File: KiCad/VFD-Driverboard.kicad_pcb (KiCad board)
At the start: 2 copper layers, 100 x 25 mm, 2 parts, among them J2 Breadboard

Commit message: new PCB
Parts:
- removed J2: Breadboard, Connector_PinHeader_2.54mm:PinHeader_1x10_P2.54mm_Vertical
- added C1: 1u, Capacitor_SMD:C_2220_5750Metric_Pad1.97x5.40mm_HandSolder, B.Cu at (35.1, 27.5)
- added C2: 10n, Capacitor_SMD:C_1206_3216Metric_Pad1.33x1.80mm_HandSolder, B.Cu at (53.3, 32.4)
- added C3: 1u, Capacitor_SMD:C_2220_5750Metric_Pad1.97x5.40mm_HandSolder, B.Cu at (107.2, 30.3)
- added C4: 1u, Capacitor_SMD:C_2220_5750Metric_Pad1.97x5.40mm_HandSolder, B.Cu at (21.1, 30.2)
- added C5: 1u, Capacitor_SMD:C_2220_5750Metric_Pad1.97x5.40mm_HandSolder, B.Cu at (54.7, 24.0)
- added C6: 100uF, Capacitor_Tantalum_SMD:CP_EIA-7343-31_Kemet-D_Pad2.25x2.55mm_HandSolder, B.Cu at (64.2, 34.5)
- added C7: 270pF, Capacitor_SMD:C_1206_3216Metric_Pad1.33x1.80mm_HandSolder, B.Cu at (76.5, 38.0)
- added C8: 100uF, Capacitor_Tantalum_SMD:CP_EIA-7343-31_Kemet-D_Pad2.25x2.55mm_HandSolder, B.Cu at (99.6, 34.6)
- added C9: 82p, Capacitor_SMD:C_1206_3216Metric_Pad1.33x1.80mm_HandSolder, F.Cu at (93.3, 24.9)
- added D1: 2V7, Diode_SMD:D_2010_5025Metric_Pad1.52x2.65mm_HandSolder, B.Cu at (63.2, 22.6)
- added D2: 1N5819, Diode_SMD:D_SOD-123, B.Cu at (93.4, 31.2)
- added D3: D, Diode_SMD:D_2010_5025Metric_Pad1.52x2.65mm_HandSolder, B.Cu at (63.2, 27.1)
- added G***: LOGO, MyLib:Salamander_Silk, F.Cu at (105.0, 32.5)
- added G***: LOGO, MyLib:Salamander_B_Copper, F.Cu at (32.0, 33.6)
- added H1: MountingHole, MountingHole:MountingHole_3.2mm_M3_ISO14580_Pad_TopBottom, F.Cu at (17.2, 17.0)
- added H2: MountingHole, MountingHole:MountingHole_3.2mm_M3_ISO14580_Pad_TopBottom, F.Cu at (109.7, 17.0)
- added H3: MountingHole, MountingHole:MountingHole_3.2mm_M3_ISO14580_Pad_TopBottom, F.Cu at (17.2, 45.0)
- added H4: MountingHole, MountingHole:MountingHole_3.2mm_M3_ISO14580_Pad_TopBottom, F.Cu at (109.5, 45.0)
- added J1: MCU, Connector_PinSocket_2.54mm:PinSocket_1x08_P2.54mm_Vertical, F.Cu at (100.2, 16.4)
- added L1: 100uH, MyLib:IND_TAIYO_NRS8040_TAY, B.Cu at (77.8, 24.5)
- added R1: 10k, Resistor_SMD:R_1206_3216Metric_Pad1.30x1.75mm_HandSolder, B.Cu at (43.9, 32.3)
- added R10: 47k, Resistor_SMD:R_1206_3216Metric_Pad1.30x1.75mm_HandSolder, F.Cu at (99.6, 24.9)
- added R11: 1k8, Resistor_SMD:R_1206_3216Metric_Pad1.30x1.75mm_HandSolder, F.Cu at (99.6, 28.5)
- added R12: 8k2, Resistor_SMD:R_1206_3216Metric_Pad1.30x1.75mm_HandSolder, F.Cu at (93.3, 28.5)
- added R2: 10k, Resistor_SMD:R_1206_3216Metric_Pad1.30x1.75mm_HandSolder, B.Cu at (53.3, 28.8)
- added R3: 2k2, Resistor_SMD:R_1206_3216Metric_Pad1.30x1.75mm_HandSolder, B.Cu at (43.9, 35.9)
- added R4: 10k, Resistor_SMD:R_1206_3216Metric_Pad1.30x1.75mm_HandSolder, B.Cu at (43.9, 22.2)
- added R5: 1k, Resistor_SMD:R_1206_3216Metric_Pad1.30x1.75mm_HandSolder, F.Cu at (107.2, 24.9)
- added R6: 1k, Resistor_SMD:R_1206_3216Metric_Pad1.30x1.75mm_HandSolder, F.Cu at (21.1, 24.8)
- added R7: 100k, Resistor_SMD:R_1206_3216Metric_Pad1.30x1.75mm_HandSolder, B.Cu at (53.3, 35.9)
- added R8: 1, Resistor_SMD:R_1206_3216Metric_Pad1.30x1.75mm_HandSolder, B.Cu at (70.3, 38.0)
- added R9: 180, Resistor_SMD:R_1206_3216Metric_Pad1.30x1.75mm_HandSolder, B.Cu at (70.2, 34.5)
- added TP1: VEE, TestPoint:TestPoint_Pad_D2.5mm, B.Cu at (63.4, 16.9)
- added TP2: F-, TestPoint:TestPoint_Pad_D2.5mm, B.Cu at (104.2, 17.0)
- added TP3: F+, TestPoint:TestPoint_Pad_D2.5mm, B.Cu at (23.3, 16.9)
- added U1: MC34063, MyLib:SOIC127P599X175-8N, B.Cu at (77.7, 32.9)
- added U2: LM4871, MyLib:SOIC127P599X175-8N, B.Cu at (44.0, 27.2)
- V1: value ~ -> HCS-12SS59T
- moved V1 5.44 mm to (13.4, 19.4)
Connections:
- V1 pad 7: GNDD -> Gnd
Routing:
- net Net-(D1-K): track 0.00 -> 99.3 mm, vias 0 -> 4
- net Net-(U2-V01): track 0.00 -> 90.2 mm, vias 0 -> 2
- net VCC: track 35.2 -> 88.6 mm, vias 0 -> 1
- net Net-(D3-K): track 0.00 -> 48.1 mm
- net Gnd: track 0.00 -> 46.5 mm
- net Net-(U1-GND): track 0.00 -> 40.0 mm, vias 0 -> 1
- net GNDD: track 36.1 -> 0.00 mm
- net Net-(J1-Pin_8): track 38.8 -> 6.24 mm
- net Net-(J1-Pin_7): track 38.3 -> 6.01 mm
- net Net-(U1-Vfb): track 0.00 -> 32.3 mm, vias 0 -> 1
- net Net-(J1-Pin_6): track 37.7 -> 5.79 mm
- net Net-(J1-Pin_5): track 37.2 -> 5.57 mm
- net VF2: track 40.8 -> 16.5 mm, vias 0 -> 1
- net VF1: track 40.4 -> 16.2 mm, vias 0 -> 1
- net Net-(J1-Pin_4): track 36.7 -> 13.1 mm
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- added copper zone on B.Cu, net Gnd
- added copper zone on F.Cu, net Gnd
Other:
- board size 100 x 25 mm -> 100 x 35 mm
- board text added: "VFD driver board for Samsung HCS-12SS59T (c) 2024 rlnd HW-Rev. 1.1.0"

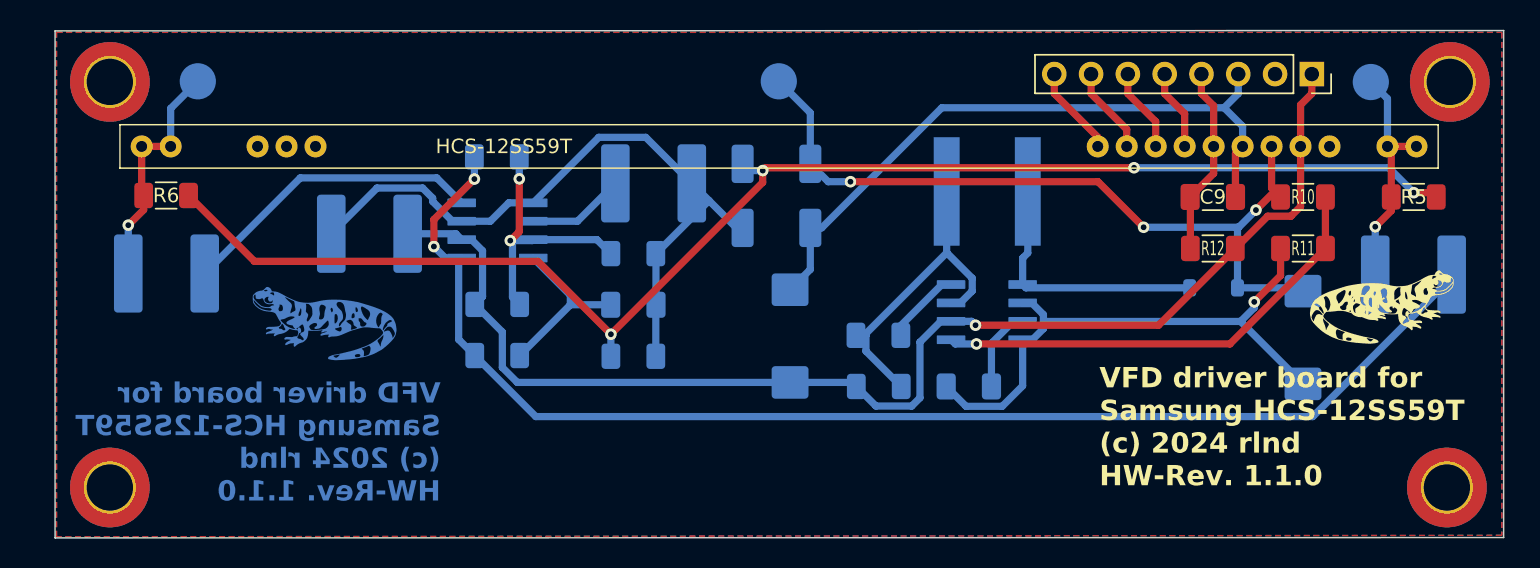
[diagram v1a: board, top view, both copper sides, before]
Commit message: added MPLAB project
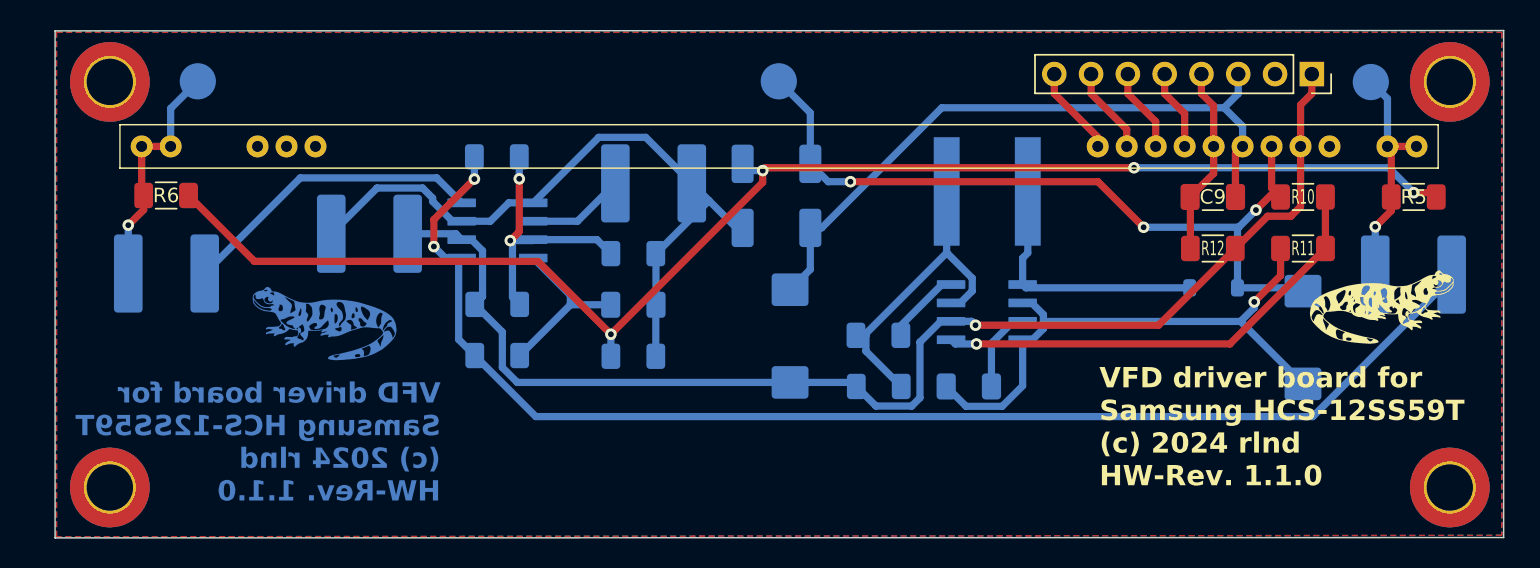
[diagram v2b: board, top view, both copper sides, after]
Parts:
- TP1: value VEE -> Vee
- U1: value MC34063 -> MC34063AD
- U2: value LM4871 -> LM4871MX_NOPB
- V1: value HCS-12SS59T -> ~
- moved H4 0.20 mm to (109.7, 45.0)
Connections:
- C1 pad 2: Net-(D3-K) -> Net-(U2-GND)
- C2 pad 2: Net-(D3-K) -> Net-(U2-GND)
- C5 pad 2: Net-(D3-K) -> Net-(U2-GND)
- J1 pad 3: Gnd -> Net-(J1-Pin_3)
- R7 pad 2: Net-(D3-K) -> Net-(U2-GND)
- U2 pad 1: Net-(D3-K) -> unconnected-(U2-SHUTDOWN-Pad1)
- U2 pad 7: Net-(D3-K) -> Net-(U2-GND)
- V1 pad 7: Gnd -> Net-(J1-Pin_3)
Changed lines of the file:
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@@
 		(allow_soldermask_bridges_in_footprints no)
 		(pcbplotparams
-			(layerselection 0x0001000_fffffffe)
+			(layerselection 0x00010fc_ffffffff)
 			(plot_on_all_layers_selection 0x0000000_00000000)
 			(disableapertmacros no)
@@
 			(viasonmask no)
 			(mode 1)
-			(useauxorigin yes)
+			(useauxorigin no)
 			(hpglpennumber 1)
 			(hpglpenspeed 20)
@@
 	(net 23 "Net-(U1-DC)")
 	(net 24 "Net-(U1-Vfb)")
+	(net 25 "Net-(U2-GND)")
+	(net 26 "Net-(J1-Pin_3)")
+	(net 27 "unconnected-(U2-SHUTDOWN-Pad1)")
 	(footprint "Resistor_SMD:R_1206_3216Metric_Pad1.30x1.75mm_HandSolder"
 		(layer "F.Cu")
@@
 	(footprint "MountingHole:MountingHole_3.2mm_M3_ISO14580_Pad_TopBottom"
 		(layer "F.Cu")
-		(at 109.4934 44.9834)
+		(at 109.6934 44.9834)
 		(descr "Mounting Hole 3.2mm, M3, ISO14580")
 		(tags "mounting hole 3.2mm m3 iso14580")
@@
 			(layers "*.Cu" "*.Mask")
 			(remove_unused_layers no)
-			(net 15 "Gnd")
+			(net 26 "Net-(J1-Pin_3)")
 			(pinfunction "Pin_3")
 			(pintype "passive")
@@
 			)
 		)
-		(property "Value" "HCS-12SS59T"
+		(property "Value" "~"
 			(at 31 2 0)
 			(unlocked yes)
@@
 			(layers "*.Cu" "*.Mask")
 			(remove_unused_layers no)
-			(net 15 "Gnd")
+			(net 26 "Net-(J1-Pin_3)")
 			(pinfunction "Gnd")
 			(pintype "passive")
@@
 			)
 		)
-		(property "Value" "MC34063"
+		(property "Value" "MC34063AD"
 			(at 0.011 -3.3948 0)
 			(layer "B.SilkS")
@@
 			)
 		)
-		(property "Value" "VEE"
+		(property "Value" "Vee"
 			(at 0 2.3622 0)
 			(layer "B.SilkS" knockout)
@@
 			(layers "B.Cu" "B.Paste" "B.Mask")
 			(roundrect_rratio 0.126582)
-			(net 10 "Net-(D3-K)")
+			(net 25 "Net-(U2-GND)")
 			(pintype "passive")
 		)
@@
 			(layers "B.Cu" "B.Paste" "B.Mask")
 			(roundrect_rratio 0.188679)
-			(net 10 "Net-(D3-K)")
+			(net 25 "Net-(U2-GND)")
 			(pintype "passive")
 		)
@@
 			(layers "B.Cu" "B.Paste" "B.Mask")
 			(roundrect_rratio 0.192308)
-			(net 10 "Net-(D3-K)")
+			(net 25 "Net-(U2-GND)")
 			(pintype "passive")
 		)
@@
 			(layers "B.Cu" "B.Paste" "B.Mask")
 			(roundrect_rratio 0.126582)
-			(net 10 "Net-(D3-K)")
+			(net 25 "Net-(U2-GND)")
 			(pintype "passive")
 		)
@@
 			)
 		)
-		(property "Value" "LM4871"
+		(property "Value" "LM4871MX_NOPB"
 			(at 0.0104 -3.3948 0)
 			(layer "B.SilkS")
@@
 			(layers "B.Cu" "B.Paste" "B.Mask")
 			(roundrect_rratio 0.07)
-			(net 10 "Net-(D3-K)")
+			(net 27 "unconnected-(U2-SHUTDOWN-Pad1)")
 			(pinfunction "SHUTDOWN")
 			(pintype "input")
@@
 			(layers "B.Cu" "B.Paste" "B.Mask")
 			(roundrect_rratio 0.07)
-			(net 10 "Net-(D3-K)")
+			(net 25 "Net-(U2-GND)")
 			(pinfunction "GND")
 			(pintype "power_in")
@@
 	(gr_text "VFD driver board for\nSamsung HCS-12SS59T\n(c) 2024 rlnd\nHW-Rev. 1.1.0"
 		(at 40.0304 46.0502 0)
-		(layer "B.Cu")
+		(layer "B.Cu" knockout)
 		(effects
 			(font
